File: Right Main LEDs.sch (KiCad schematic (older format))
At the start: 48 parts

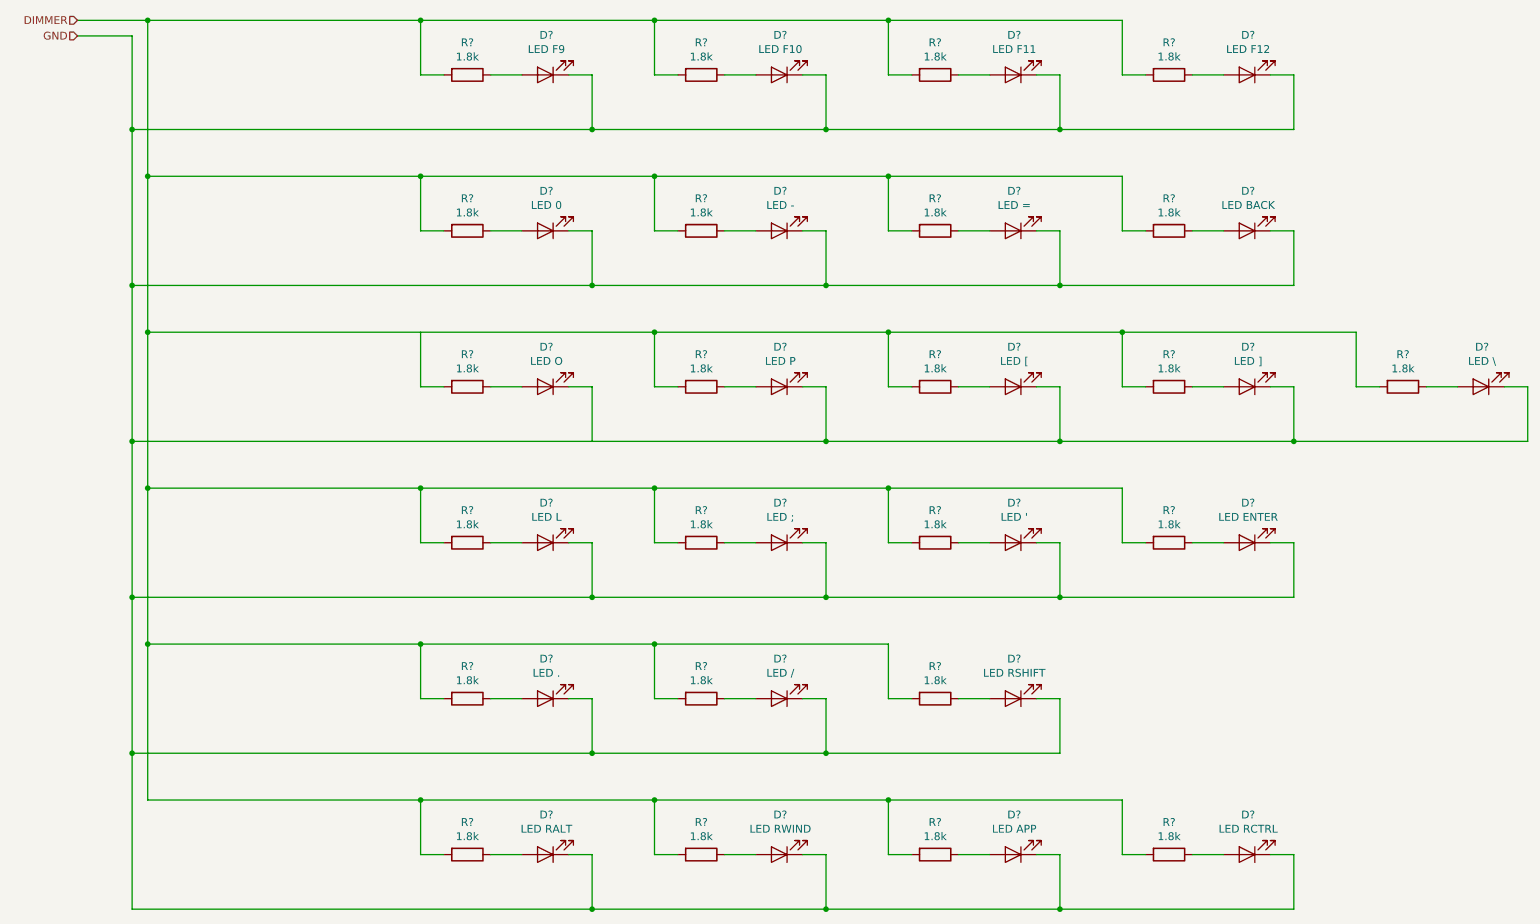
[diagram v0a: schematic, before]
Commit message: Corrected errors found in design rule check
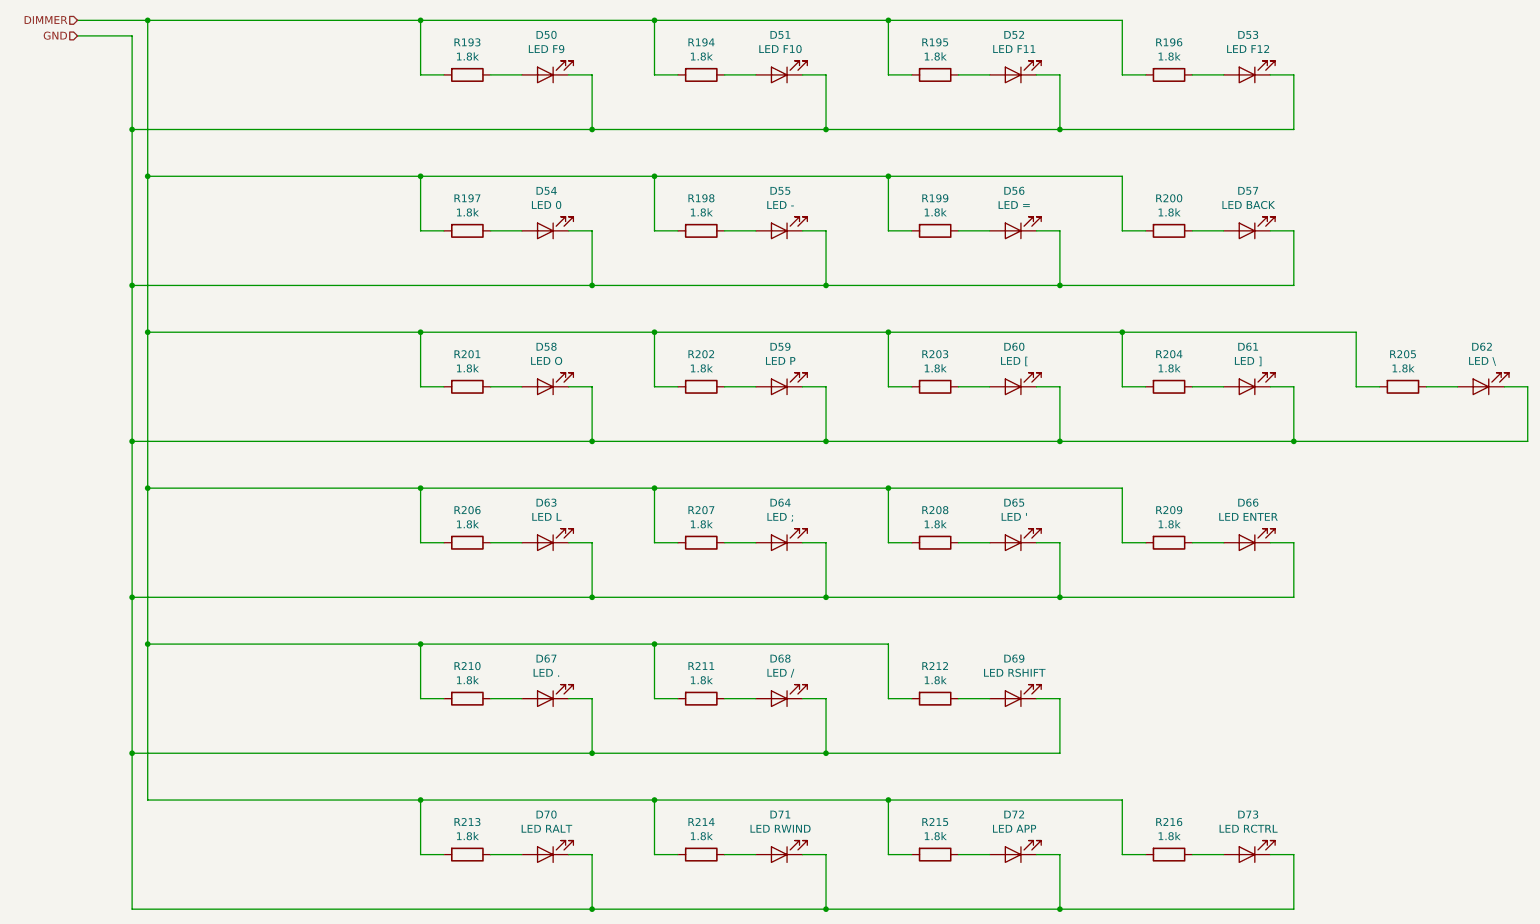
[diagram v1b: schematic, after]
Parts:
- D50, D51, D52, D53, D54, D55, D56, D57, D58, D59, D60, D61, D62, D63, D64, D65, D66, D67, D68, D69, D70, D71, D72, D73: renamed from D?; footprint (none) -> LED_SMD:LED_1206_3216Metric_ReverseMount_Hole1.8x2.4mm
- R193, R194, R195, R196, R197, R198, R199, R200, R201, R202, R203, R204, R205, R206, R207, R208, R209, R210, R211, R212, R213, R214, R215, R216: renamed from R?; footprint (none) -> Resistor_SMD:R_1206_3216Metric_Pad1.42x1.75mm_HandSolder
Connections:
- net DIMMER: now also R201.2
- net GND: now also D58.1 (K)

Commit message: Redesigned for single large PCB
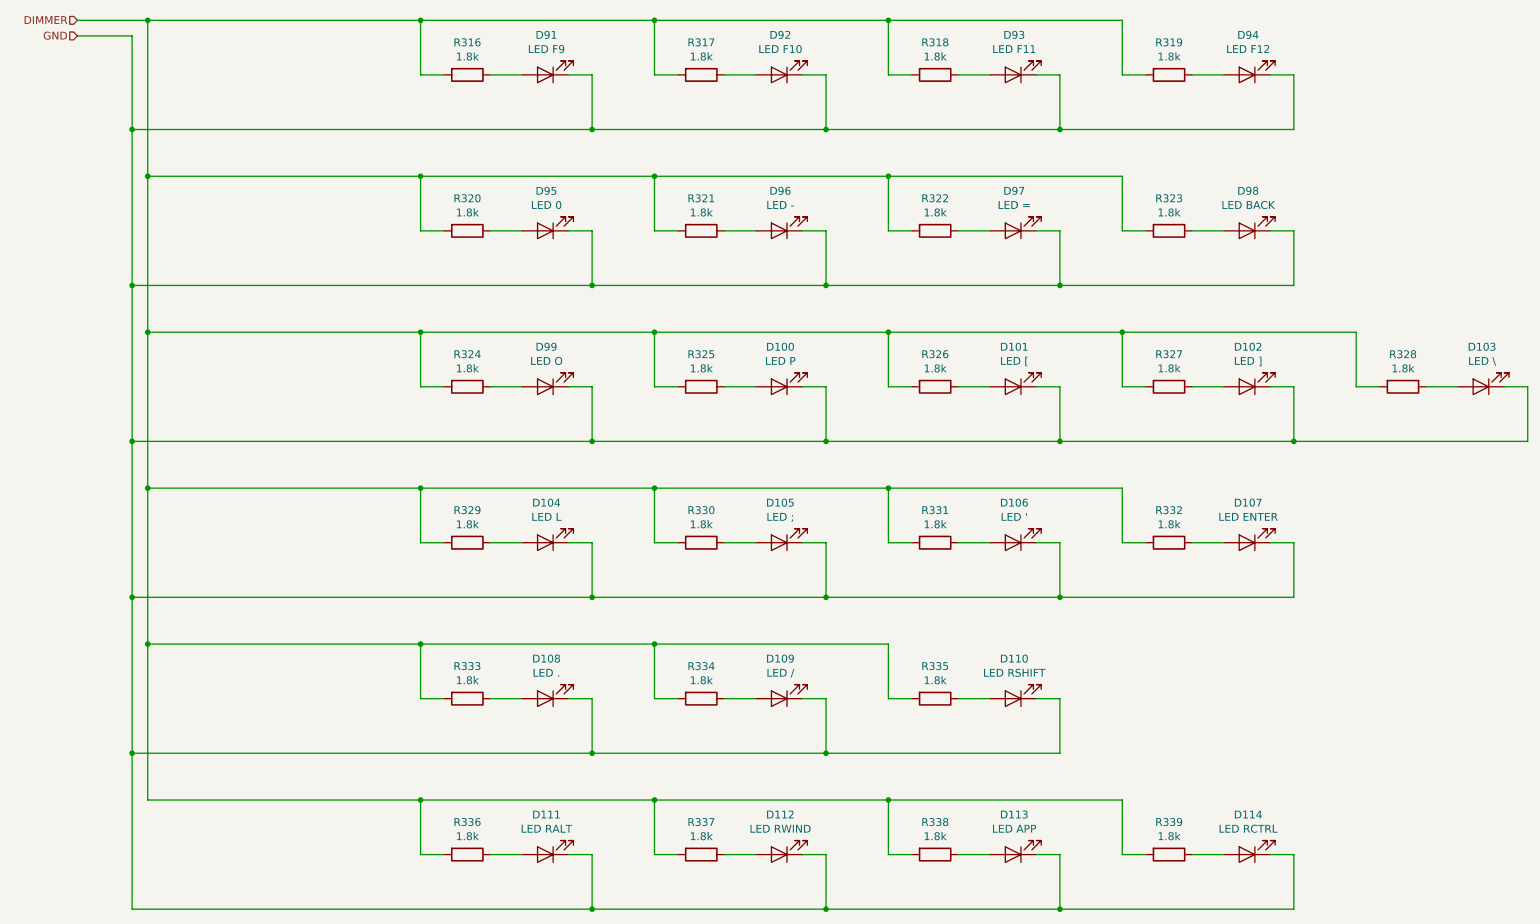
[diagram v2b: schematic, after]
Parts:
- renumbered D59 to D100, D60 to D101, D61 to D102, D62 to D103, D63 to D104, D64 to D105, D65 to D106, D66 to D107, D67 to D108, D68 to D109, D69 to D110, D70 to D111, D71 to D112, D72 to D113, D73 to D114, D50 to D91, D51 to D92, D52 to D93, D53 to D94, D54 to D95, D55 to D96, D56 to D97, D57 to D98, D58 to D99, R193 to R316, R194 to R317, R195 to R318, R196 to R319, R197 to R320, R198 to R321, R199 to R322, R200 to R323, R201 to R324, R202 to R325, R203 to R326, R204 to R327, R205 to R328, R206 to R329, R207 to R330, R208 to R331, R209 to R332, R210 to R333, R211 to R334, R212 to R335, R213 to R336, R214 to R337, R215 to R338, R216 to R339
